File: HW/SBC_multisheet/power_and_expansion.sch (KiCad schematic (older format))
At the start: 3 parts

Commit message: PLUTO SBC with RTC schematics done.
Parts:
- added C10, C11, C12, C13, C14, C15, C16, C9: .1uF, symbol C_Small
- added J4: POWER IN, symbol CONN_01X02
- added J5: Expansion Port, symbol CONN_02X25
- C7: renamed from 10uF; value CP1_Small -> 100 uF
- C8: renamed from 10uF; value CP1_Small -> 10 uF
- gave numbers to parts that had none: 1
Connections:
- net VCC is gone; now on net GND: C8.1, U11.VO
- net +9V: now also J4.2 (P2)
- net GND: now also C10.1, C10.2, C11.1, C11.2, C12.1, C12.2, C13.1, C13.2, C14.1, C14.2, C15.1, C15.2, C16.1, C16.2, C9.1, C9.2, J4.1 (P1), J5.1 (P1), J5.2 (P2), J5.49 (P49), J5.50 (P50)
- new net A0: J5.21 (P21)
- new net A1: J5.19 (P19)
- new net A10: J5.18 (P18)
- new net A11: J5.14 (P14)
- new net A12: J5.5 (P5)
- new net A13: J5.8 (P8)
- new net A14: J5.3 (P3)
- new net A15: J5.32 (P32)
- new net A2: J5.17 (P17)
- new net A3: J5.15 (P15)
- new net A4: J5.13 (P13)
- new net A5: J5.11 (P11)
- new net A6: J5.9 (P9)
- new net A7: J5.7 (P7)
- new net A8: J5.10 (P10)
- new net A9: J5.12 (P12)
- new net D0: J5.23 (P23)
- new net D1: J5.25 (P25)
- new net D2: J5.27 (P27)
- new net D3: J5.30 (P30)
- new net D4: J5.28 (P28)
- new net D5: J5.26 (P26)
- new net D6: J5.24 (P24)
- new net D7: J5.22 (P22)
- new net R/~W: J5.43 (P43)
- new net ~7F0X: J5.34 (P34)
- new net ~7F2X: J5.36 (P36)
- new net ~7F4X: J5.38 (P38)
- new net ~7F6X: J5.40 (P40)
- new net ~7F8X: J5.42 (P42)
- new net ~7FXX: J5.39 (P39)
- new net ~CLK: J5.35 (P35)
- new net ~IRQ: J5.37 (P37)
- new net ~MRD: J5.16 (P16)
- new net ~MWR: J5.6 (P6)
- new net ~NMI: J5.41 (P41)
- new net ~RES: J5.33 (P33)
- no-connect marks 0 -> 9

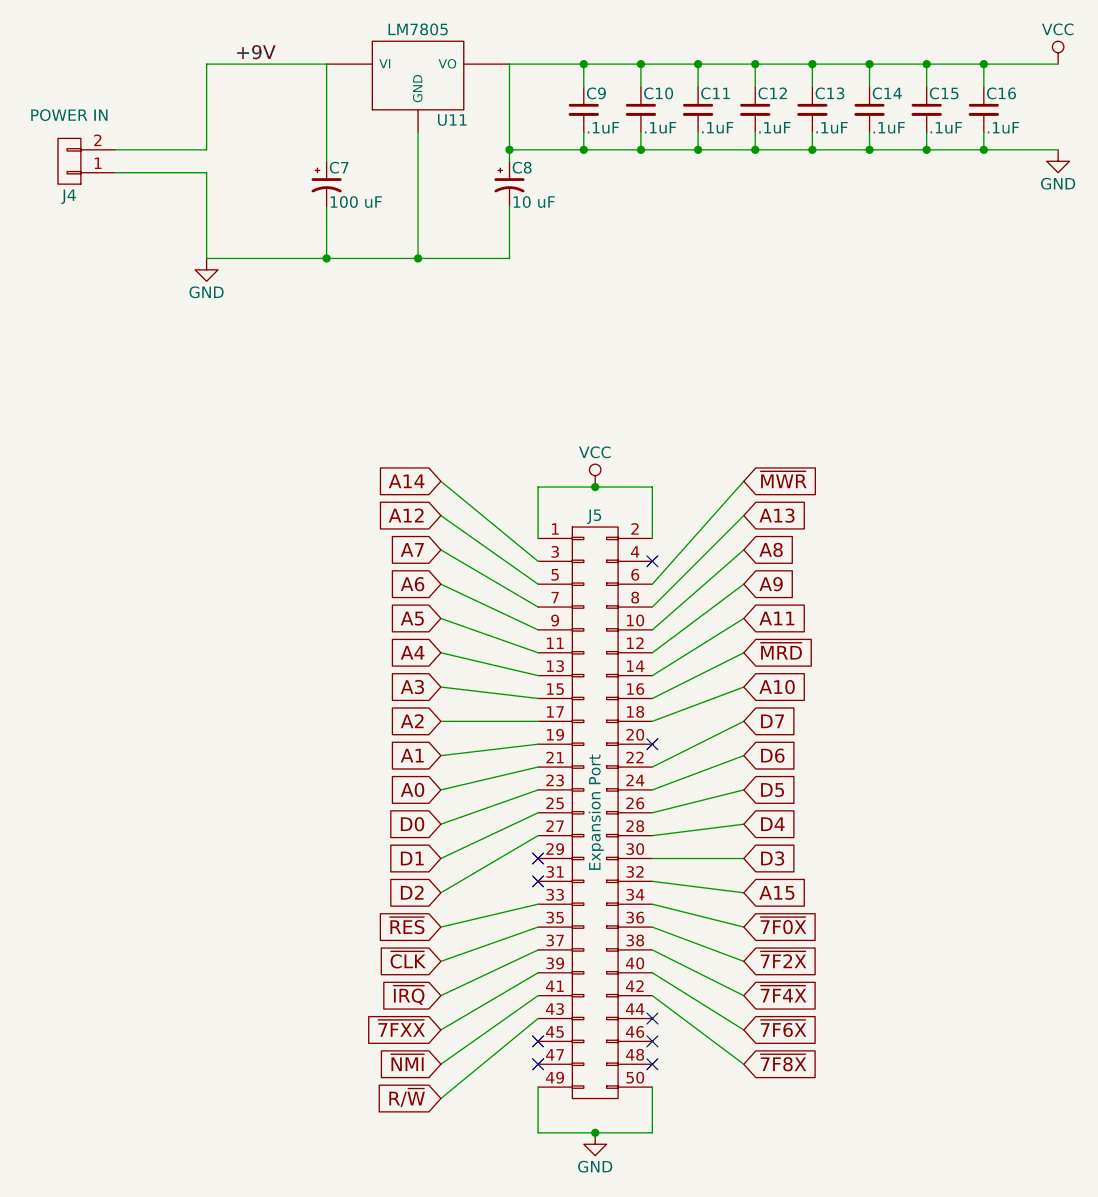
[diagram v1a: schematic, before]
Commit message: The PCB layout editor doesn't like 7805's footprint.
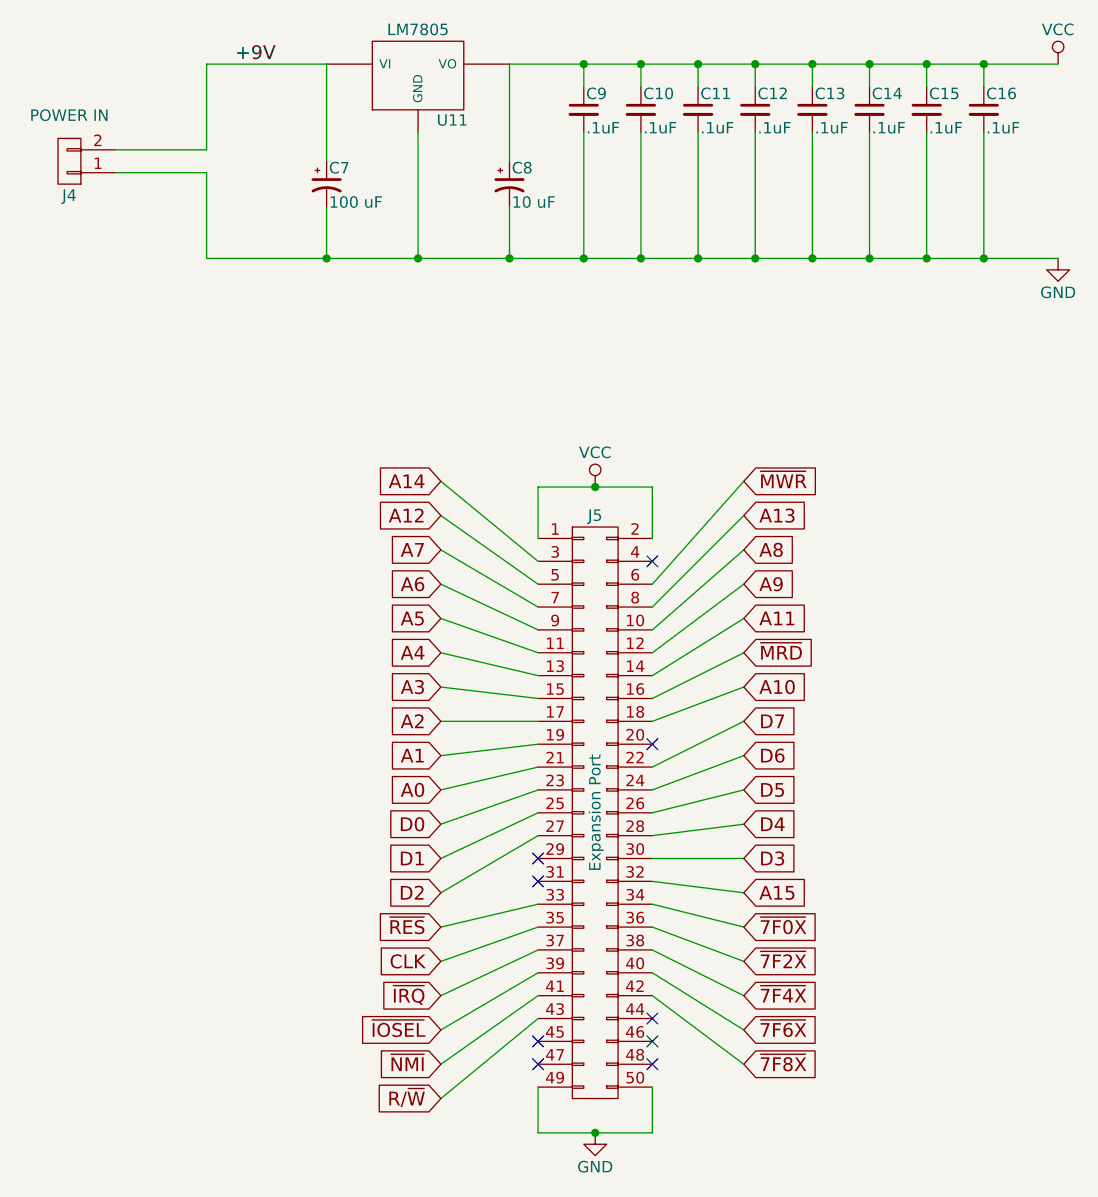
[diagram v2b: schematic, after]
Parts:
- C10, C11, C12, C13, C14, C15, C16, C9: footprint (none) -> Capacitors_ThroughHole:C_Disc_D3.8mm_W2.6mm_P2.50mm
- C7: footprint (none) -> Capacitors_ThroughHole:CP_Radial_D6.3mm_P2.50mm
- C8: footprint (none) -> Capacitors_ThroughHole:CP_Radial_D5.0mm_P2.00mm
- J4: footprint (none) -> Pin_Headers:Pin_Header_Straight_1x02_Pitch2.54mm
- J5: footprint (none) -> Pin_Headers:Pin_Header_Straight_2x25_Pitch2.54mm
- U11: footprint (none) -> TO_SOT_Packages_THT:TO-220_Vertical
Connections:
- net GND: no longer C10.1, C11.1, C12.1, C13.1, C14.1, C15.1, C16.1, C8.1, C9.1, J5.1 (P1), J5.2 (P2), U11.VO
- net ~7FXX renamed ~IOSEL
- net ~CLK renamed CLK
- new net VCC: C10.1, C11.1, C12.1, C13.1, C14.1, C15.1, C16.1, C8.1, C9.1, J5.1 (P1), J5.2 (P2), U11.VO
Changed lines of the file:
@@
 F 0 "U11" H 2975 1504 50  0000 C CNN
 F 1 "LM7805" H 2825 1900 50  0000 C CNN
-F 2 "" H 2825 1700 50  0001 C CNN
+F 2 "TO_SOT_Packages_THT:TO-220_Vertical" H 2825 1700 50  0001 C CNN
 F 3 "" H 2825 1700 50  0001 C CNN
 	1    2825 1700
@@
 F 0 "C7" H 2435 2245 50  0000 L CNN
 F 1 "100 uF" H 2435 2095 50  0000 L CNN
-F 2 "" H 2425 2175 50  0001 C CNN
+F 2 "Capacitors_ThroughHole:CP_Radial_D6.3mm_P2.50mm" H 2425 2175 50  0001 C CNN
 F 3 "" H 2425 2175 50  0001 C CNN
 	1    2425 2175
@@
 F 0 "C8" H 3235 2245 50  0000 L CNN
 F 1 "10 uF" H 3235 2095 50  0000 L CNN
-F 2 "" H 3225 2175 50  0001 C CNN
+F 2 "Capacitors_ThroughHole:CP_Radial_D5.0mm_P2.00mm" H 3225 2175 50  0001 C CNN
 F 3 "" H 3225 2175 50  0001 C CNN
 	1    3225 2175
@@
 $EndComp
 $Comp
-L GND #PWR22
-U 1 1 58D5ED53
-P 1900 2500
-F 0 "#PWR22" H 1900 2250 50  0001 C CNN
-F 1 "GND" H 1900 2350 50  0000 C CNN
-F 2 "" H 1900 2500 50  0001 C CNN
-F 3 "" H 1900 2500 50  0001 C CNN
-	1    1900 2500
-	1    0    0    -1
-$EndComp
-$Comp
-L VCC #PWR25
+L VCC #PWR028
 U 1 1 58D5EE10
 P 5625 1650
-F 0 "#PWR25" H 5625 1500 50  0001 C CNN
+F 0 "#PWR028" H 5625 1500 50  0001 C CNN
 F 1 "VCC" H 5625 1800 50  0000 C CNN
 F 2 "" H 5625 1650 50  0001 C CNN
@@
 F 0 "J4" H 1300 2225 50  0000 C CNN
 F 1 "POWER IN" H 1300 1875 50  0000 C CNN
-F 2 "" H 1300 2075 50  0001 C CNN
+F 2 "Pin_Headers:Pin_Header_Straight_1x02_Pitch2.54mm" H 1300 2075 50  0001 C CNN
 F 3 "" H 1300 2075 50  0001 C CNN
 	1    1300 2075
@@
 F 0 "C9" H 3560 1920 50  0000 L CNN
 F 1 ".1uF" H 3560 1770 50  0000 L CNN
-F 2 "" H 3550 1850 50  0001 C CNN
+F 2 "Capacitors_ThroughHole:C_Disc_D3.8mm_W2.6mm_P2.50mm" H 3550 1850 50  0001 C CNN
 F 3 "" H 3550 1850 50  0001 C CNN
 	1    3550 1850
@@
 F 0 "C10" H 3810 1920 50  0000 L CNN
 F 1 ".1uF" H 3810 1770 50  0000 L CNN
-F 2 "" H 3800 1850 50  0001 C CNN
+F 2 "Capacitors_ThroughHole:C_Disc_D3.8mm_W2.6mm_P2.50mm" H 3800 1850 50  0001 C CNN
 F 3 "" H 3800 1850 50  0001 C CNN
 	1    3800 1850
@@
 F 0 "C11" H 4060 1920 50  0000 L CNN
 F 1 ".1uF" H 4060 1770 50  0000 L CNN
-F 2 "" H 4050 1850 50  0001 C CNN
+F 2 "Capacitors_ThroughHole:C_Disc_D3.8mm_W2.6mm_P2.50mm" H 4050 1850 50  0001 C CNN
 F 3 "" H 4050 1850 50  0001 C CNN
 	1    4050 1850
@@
 F 0 "C14" H 4810 1920 50  0000 L CNN
 F 1 ".1uF" H 4810 1770 50  0000 L CNN
-F 2 "" H 4800 1850 50  0001 C CNN
+F 2 "Capacitors_ThroughHole:C_Disc_D3.8mm_W2.6mm_P2.50mm" H 4800 1850 50  0001 C CNN
 F 3 "" H 4800 1850 50  0001 C CNN
 	1    4800 1850
@@
 F 0 "C12" H 4310 1920 50  0000 L CNN
 F 1 ".1uF" H 4310 1770 50  0000 L CNN
-F 2 "" H 4300 1850 50  0001 C CNN
+F 2 "Capacitors_ThroughHole:C_Disc_D3.8mm_W2.6mm_P2.50mm" H 4300 1850 50  0001 C CNN
 F 3 "" H 4300 1850 50  0001 C CNN
 	1    4300 1850
@@
 F 0 "C13" H 4560 1920 50  0000 L CNN
 F 1 ".1uF" H 4560 1770 50  0000 L CNN
-F 2 "" H 4550 1850 50  0001 C CNN
+F 2 "Capacitors_ThroughHole:C_Disc_D3.8mm_W2.6mm_P2.50mm" H 4550 1850 50  0001 C CNN
 F 3 "" H 4550 1850 50  0001 C CNN
 	1    4550 1850
@@
 F 0 "C16" H 5310 1920 50  0000 L CNN
 F 1 ".1uF" H 5310 1770 50  0000 L CNN
-F 2 "" H 5300 1850 50  0001 C CNN
+F 2 "Capacitors_ThroughHole:C_Disc_D3.8mm_W2.6mm_P2.50mm" H 5300 1850 50  0001 C CNN
 F 3 "" H 5300 1850 50  0001 C CNN
 	1    5300 1850
@@
 F 0 "C15" H 5060 1920 50  0000 L CNN
 F 1 ".1uF" H 5060 1770 50  0000 L CNN
-F 2 "" H 5050 1850 50  0001 C CNN
+F 2 "Capacitors_ThroughHole:C_Disc_D3.8mm_W2.6mm_P2.50mm" H 5050 1850 50  0001 C CNN
 F 3 "" H 5050 1850 50  0001 C CNN
 	1    5050 1850
-	1    0    0    -1
-$EndComp
-$Comp
-L GND #PWR26
-U 1 1 58D7579D
-P 5625 2025
-F 0 "#PWR26" H 5625 1775 50  0001 C CNN
-F 1 "GND" H 5625 1875 50  0000 C CNN
-F 2 "" H 5625 2025 50  0001 C CNN
-F 3 "" H 5625 2025 50  0001 C CNN
-	1    5625 2025
 	1    0    0    -1
 $EndComp
@@
 F 0 "J5" H 3600 6225 50  0000 C CNN
 F 1 "Expansion Port" V 3600 4925 50  0000 C CNN
-F 2 "" H 3600 4175 50  0001 C CNN
+F 2 "Pin_Headers:Pin_Header_Straight_2x25_Pitch2.54mm" H 3600 4175 50  0001 C CNN
 F 3 "" H 3600 4175 50  0001 C CNN
 	1    3600 4925
@@
 	2425 2275 2425 2500
 Wire Wire Line
-	1900 2500 3225 2500
+	1900 2500 5625 2500
 Wire Wire Line
 	3225 2500 3225 2275
@@
 	3225 1650 5625 1650
 Wire Wire Line
-	3225 2025 5625 2025
-Connection ~ 3225 2025
-Wire Wire Line
 	3550 1750 3550 1650
 Connection ~ 3550 1650
 Wire Wire Line
-	3550 1950 3550 2025
-Connection ~ 3550 2025
+	3550 1950 3550 2500
 Wire Wire Line
 	3800 1750 3800 1650
 Connection ~ 3800 1650
 Wire Wire Line
-	3800 1950 3800 2025
-Connection ~ 3800 2025
+	3800 1950 3800 2500
 Wire Wire Line
 	4050 1750 4050 1650
 Connection ~ 4050 1650
 Wire Wire Line
-	4050 1950 4050 2025
-Connection ~ 4050 2025
+	4050 1950 4050 2500
 Wire Wire Line
 	4300 1750 4300 1650
 Connection ~ 4300 1650
 Wire Wire Line
-	4300 1950 4300 2025
-Connection ~ 4300 2025
+	4300 1950 4300 2500
 Wire Wire Line
 	4550 1750 4550 1650
 Connection ~ 4550 1650
 Wire Wire Line
-	4550 1950 4550 2025
-Connection ~ 4550 2025
+	4550 1950 4550 2500
 Wire Wire Line
 	4800 1750 4800 1650
 Connection ~ 4800 1650
 Wire Wire Line
-	4800 1950 4800 2025
-Connection ~ 4800 2025
+	4800 1950 4800 2500
 Wire Wire Line
 	5050 1750 5050 1650
 Connection ~ 5050 1650
 Wire Wire Line
-	5050 1950 5050 2025
-Connection ~ 5050 2025
+	5050 1950 5050 2500
 Wire Wire Line
 	5300 1750 5300 1650
 Connection ~ 5300 1650
 Wire Wire Line
-	5300 1950 5300 2025
-Connection ~ 5300 2025
-$Comp
-L VCC #PWR23
+	5300 1950 5300 2500
+$Comp
+L VCC #PWR029
 U 1 1 58D7686C
 P 3600 3500
-F 0 "#PWR23" H 3600 3350 50  0001 C CNN
+F 0 "#PWR029" H 3600 3350 50  0001 C CNN
 F 1 "VCC" H 3600 3650 50  0000 C CNN
 F 2 "" H 3600 3500 50  0001 C CNN
@@
 Connection ~ 3600 3500
 $Comp
-L GND #PWR24
+L GND #PWR030
 U 1 1 58D76B4A
 P 3600 6325
-F 0 "#PWR24" H 3600 6075 50  0001 C CNN
+F 0 "#PWR030" H 3600 6075 50  0001 C CNN
 F 1 "GND" H 3600 6175 50  0000 C CNN
 F 2 "" H 3600 6325 50  0001 C CNN
@@
 D7
 Text GLabel 2925 5575 0    60   Input ~ 0
-~CLK
+CLK
 Text GLabel 2925 5725 0    60   Input ~ 0
 ~IRQ
 Text GLabel 2925 5875 0    60   Input ~ 0
-~7FXX
+~IOSEL
 Text GLabel 2925 6025 0    60   Input ~ 0
 ~NMI
@@
 NoConn ~ 3850 5925
 NoConn ~ 3850 6025
+Connection ~ 3225 2500
+Connection ~ 3550 2500
+Connection ~ 3800 2500
+Connection ~ 4050 2500
+Connection ~ 4300 2500
+Connection ~ 4550 2500
+Connection ~ 4800 2500
+Connection ~ 5050 2500
+Connection ~ 5300 2500
+$Comp
+L GND #PWR031
+U 1 1 58D85868
+P 5625 2500
+F 0 "#PWR031" H 5625 2250 50  0001 C CNN
+F 1 "GND" H 5625 2350 50  0000 C CNN
+F 2 "" H 5625 2500 50  0001 C CNN
+F 3 "" H 5625 2500 50  0001 C CNN
+	1    5625 2500
+	1    0    0    -1
+$EndComp
 $EndSCHEMATC
